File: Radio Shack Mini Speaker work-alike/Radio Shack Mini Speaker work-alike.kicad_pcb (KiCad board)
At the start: 2 copper layers, 1.2 x 12 mm, 16 parts, among them J1 input, J2 aux speaker out, Q1 2SC1815, SW1 SW_SPDT, U1 LM386

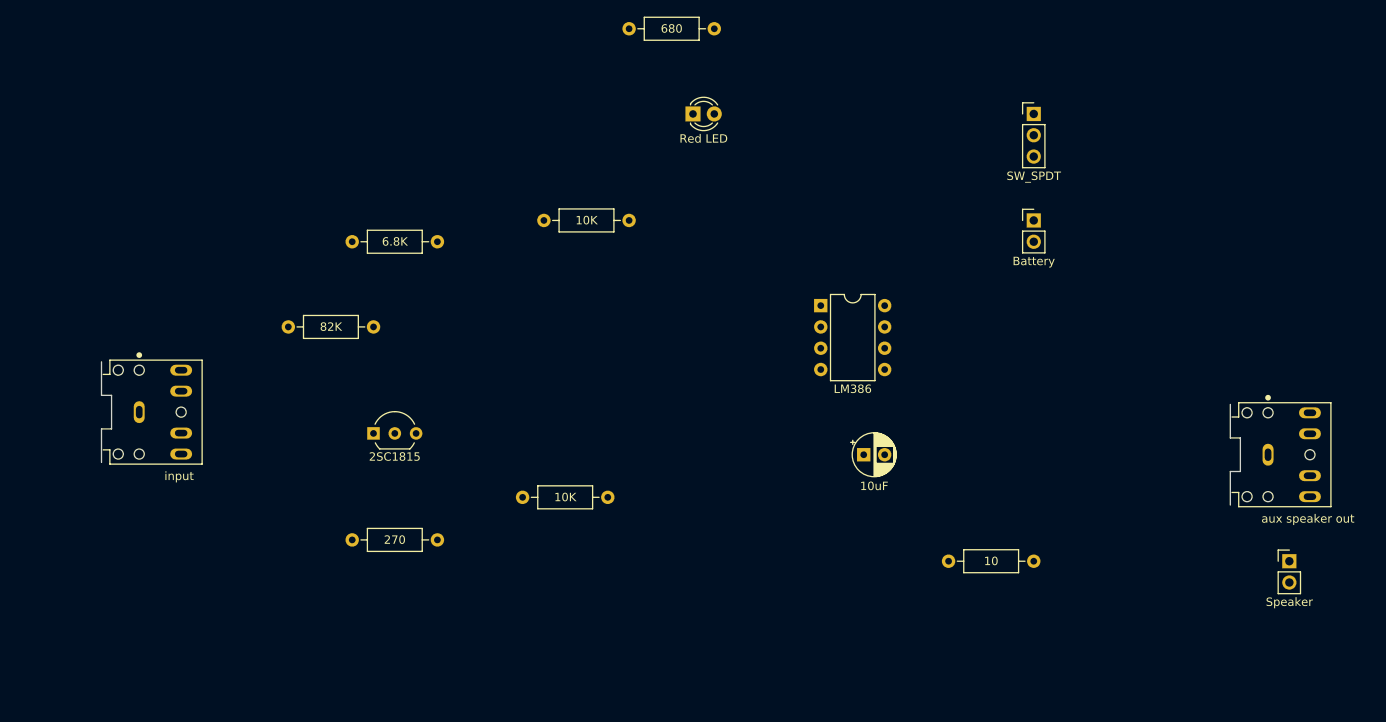
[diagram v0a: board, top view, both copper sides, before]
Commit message: updated switch position
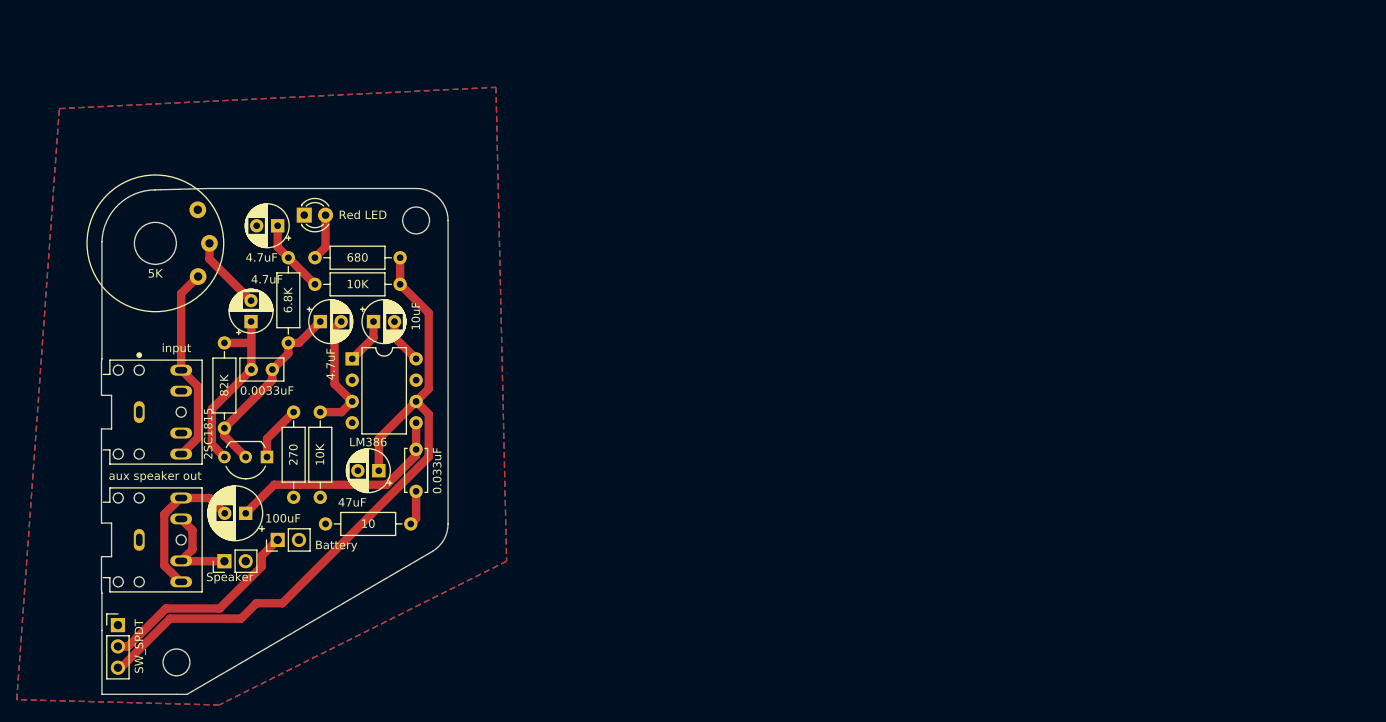
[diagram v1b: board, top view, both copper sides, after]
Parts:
- added C1: 0.0033uF, Capacitor_THT:C_Disc_D5.0mm_W2.5mm_P2.50mm, F.Cu at (69.3, 63.5)
- added C2: 0.033uF, Capacitor_THT:C_Disc_D5.0mm_W2.5mm_P5.00mm, F.Cu at (88.9, 73.0)
- added C3: 4.7uF, Capacitor_THT:CP_Radial_D5.0mm_P2.50mm, F.Cu at (69.2, 57.8)
- added C4: 4.7uF, Capacitor_THT:CP_Radial_D5.0mm_P2.50mm, F.Cu at (77.5, 57.8)
- added C5: 4.7uF, Capacitor_THT:CP_Radial_D5.0mm_P2.50mm, F.Cu at (72.4, 46.4)
- added C7: 47uF, Capacitor_THT:CP_Radial_D5.0mm_P2.50mm, F.Cu at (84.5, 75.6)
- added C8: 100uF, Capacitor_THT:CP_Radial_D6.3mm_P2.50mm, F.Cu at (68.6, 80.6)
- added G***: LOGO, Evan's parts:OSHW gear, B.Cu at (81.9, 52.1)
- added G***: LOGO, Evan's parts:Evan Logo, B.Cu at (76.2, 73.0)
- added REF**: MountingHole_3.2mm_M3, MountingHole:MountingHole_3.2mm_M3, F.Cu at (60.3, 98.4)
- added REF**: MountingHole_3.2mm_M3, MountingHole:MountingHole_3.2mm_M3, F.Cu at (88.9, 45.7)
- added RV1: 5K, Evan's parts:allen bradlet thumbwheel pot, F.Cu at (57.8, 48.5)
- moved J2 135.0 mm to (55.9, 83.8)
- moved LS1 127.0 mm to (66.0, 86.4), turned to 90 degrees
- moved SW1 125.1 mm to (53.3, 94.0)
- moved BT1 97.9 mm to (72.4, 83.8), turned to 90 degrees
- moved R6 64.3 mm to (88.3, 81.9), turned to 180 degrees
- moved C6 60.6 mm to (83.8, 57.8)
- moved U1 56.2 mm to (81.3, 62.2)
- moved D1 47.9 mm to (75.6, 45.1)
- moved R7 38.6 mm to (87.0, 50.2), turned to 180 degrees
- moved R5 26.2 mm to (77.5, 68.6), turned to -90 degrees
- moved R3 18.8 mm to (87.0, 53.3), turned to 180 degrees
- moved R4 16.8 mm to (74.3, 68.6), turned to -90 degrees
- moved R2 14.3 mm to (73.7, 60.3), turned to 90 degrees
- moved Q1 13.0 mm to (71.1, 73.9), turned to 180 degrees
- moved R1 7.85 mm to (66.0, 60.3), turned to -90 degrees
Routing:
- net VCC: track 0.00 -> 84.0 mm
- net Net-(Q1-B): track 0.00 -> 27.6 mm
- net Net-(C2-Pad1): track 0.00 -> 27.1 mm
- net Net-(BT1-+): track 0.00 -> 25.1 mm
- net Net-(J1-Pad2): track 0.00 -> 23.8 mm
- net Net-(Q1-C): track 0.00 -> 22.7 mm
- net Net-(C8-Pad2): track 0.00 -> 18.4 mm
- net Net-(U1-+): track 0.00 -> 15.1 mm
- net Net-(J2-Pad10): track 0.00 -> 11.4 mm
- net Net-(C3-Pad2): track 0.00 -> 8.89 mm
- net Net-(C5-Pad1): track 0.00 -> 8.83 mm
- net Net-(Q1-E): track 0.00 -> 6.67 mm
- net Net-(D1-A): track 0.00 -> 5.60 mm
- net Net-(C6-Pad2): track 0.00 -> 5.51 mm
- net Net-(C6-Pad1): track 0.00 -> 5.50 mm
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- added copper zone on B.Cu, net GND
- added copper zone on F.Cu, net GND
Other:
- board size 1.2 x 12 mm -> 41.3 x 60.3 mm
- board text added: "Archer mini amplified speaker"
- board text added: "abzman2k.wordpress.com"
- board text added: "now with power LED!"
- board text added: "work-alike"

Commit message: cleaned up for fab
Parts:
- moved J2 1.90 mm to (55.9, 81.9)
- moved SW1 1.27 mm to (53.3, 92.7)
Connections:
- SW1 pad 2: Net-(BT1-+) -> VCC
- SW1 pad 3: VCC -> Net-(BT1-+)
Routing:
- net GND: track 0.00 -> 13.9 mm
- net Net-(BT1-+): track 25.1 -> 23.5 mm
- net VCC: track 84.0 -> 83.0 mm
- net Net-(J2-Pad10): track 11.4 -> 12.2 mm
- net Net-(C8-Pad2): track 18.4 -> 19.2 mm
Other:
- outline, holes or cut-outs redrawn

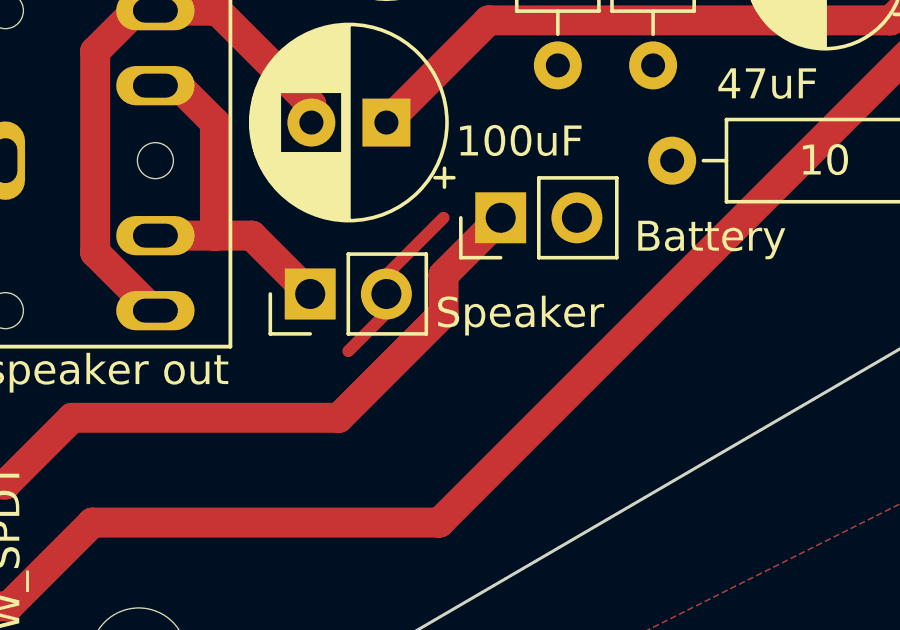
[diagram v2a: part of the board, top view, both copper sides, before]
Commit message: updated silk
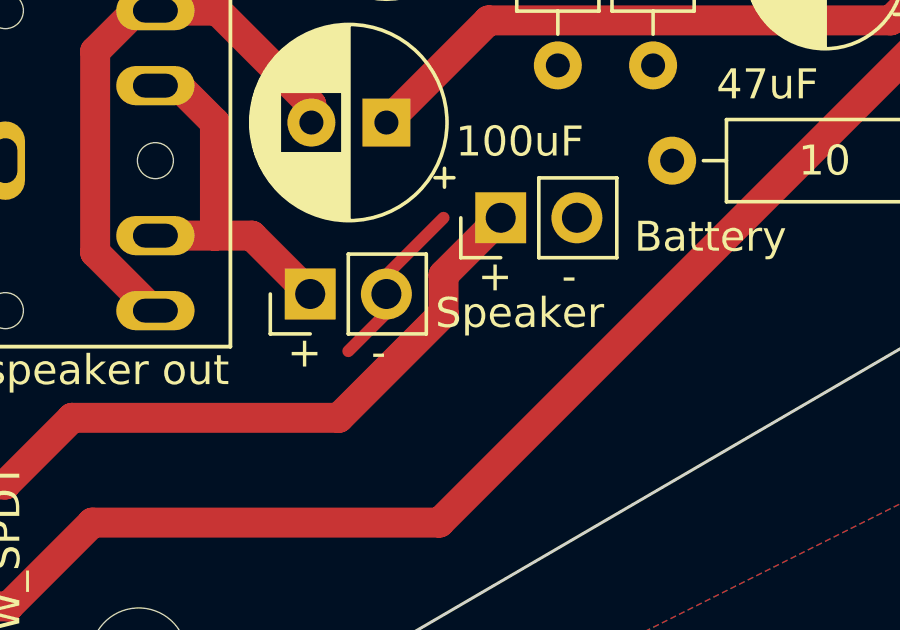
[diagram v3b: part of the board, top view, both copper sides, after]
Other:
- board text added: "+"
- board text added: "-"
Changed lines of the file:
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@@
     (effects (font (size 1 1) (thickness 0.15)) (justify left bottom mirror))
+  )
+  (gr_text "+" (at 65.278 88.9) (layer "F.SilkS")
+    (effects (font (size 1 1) (thickness 0.15)) (justify left bottom))
+  )
+  (gr_text "+" (at 71.628 86.36) (layer "F.SilkS")
+    (effects (font (size 1 1) (thickness 0.15)) (justify left bottom))
+  )
+  (gr_text "-" (at 68.072 88.9) (layer "F.SilkS")
+    (effects (font (size 1 1) (thickness 0.15)) (justify left bottom))
+  )
+  (gr_text "-" (at 74.422 86.36) (layer "F.SilkS")
+    (effects (font (size 1 1) (thickness 0.15)) (justify left bottom))
   )
   (segment (start 70.485 85.725) (end 72.39 83.82) (width 1) (layer "F.Cu") (net 1))
